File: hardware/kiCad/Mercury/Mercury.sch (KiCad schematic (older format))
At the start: 75 parts, among them J1 SWD, J10 OUTPUT, J11 Analog I/O, J12 Power Rails, J2 UART1, J3 I2C2, J4 UART1, J5 SPI1, J6 SPI2, J7 629105150521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

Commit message: Refresh
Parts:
- removed R24, R25: 22, Resistor_SMD:R_0402_1005Metric, symbol Device:R_Small
- H1, H2, H3, H4: footprint MountingHole:MountingHole_4.3mm_M4_Pad_Via -> MountingHole:MountingHole_3mm_Pad_Via
- J3: footprint Connector_Wire:SolderWire-0.1sqmm_1x04_P3.6mm_D0.4mm_OD1mm_Relief -> Connector_Wire:SolderWire-0.1sqmm_1x04_P3.6mm_D0.4mm_OD1mm
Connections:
- net ALT_INT_1: now also R8.1; no longer R9.1
- net ALT_INT_2: now also R9.1; no longer R8.1
- net FLASH_CS: now also R22.1; no longer R23.1
- net GPS_LNA_EN: now also U1.3 (PE4); no longer U1.65 (PC8)
- net I2C1_SCL: now also R5.1; no longer R4.1
- net I2C1_SDA: now also R4.1; no longer R5.1
- net SPI2_MISO: now also R23.1; no longer R21.1
- net SPI2_MOSI: now also R20.1; no longer R22.1
- net SPI2_SCK: now also R21.1; no longer R20.1
- net TIME_PULSE: now also U1.4 (PE5); no longer U1.66 (PC9)
- net USB_D+: now also J7.3 (D+)
- net USB_D-: now also J7.2 (D-)
- net ~GPS_RESET: now also U1.2 (PE3); no longer U1.67 (PA8)
- net ~GPS_SAFEBOOT: now also U1.5 (PE6); no longer U1.64 (PC7)
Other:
- moved on the sheet: J7
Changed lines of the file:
@@
 Wire Wire Line
 	5550 1000 5550 1100
+Text GLabel 8300 1250 0    50   Input ~ 0
+I2C1_SCL
 Text GLabel 8300 1150 0    50   Input ~ 0
-I2C1_SCL
-Text GLabel 8300 1250 0    50   Input ~ 0
 I2C1_SDA
 Text GLabel 9500 975  0    50   Input ~ 0
@@
 	1    0    0    -1
 $EndComp
-NoConn ~ 9675 2900
-Wire Wire Line
-	9475 2700 9425 2700
-Wire Wire Line
-	9475 2800 9425 2800
-$Comp
-L Device:R_Small R24
-U 1 1 5FE85A1A
-P 9575 2700
-F 0 "R24" V 9575 2700 50  0000 C CNN
-F 1 "22" V 9675 2700 50  0000 C CNN
-F 2 "Resistor_SMD:R_0402_1005Metric" H 9575 2700 50  0001 C CNN
-F 3 "~" H 9575 2700 50  0001 C CNN
-	1    9575 2700
-	0    -1   -1   0
-$EndComp
-$Comp
-L Device:R_Small R25
-U 1 1 5FE850CF
-P 9575 2800
-F 0 "R25" V 9575 2800 50  0000 C CNN
-F 1 "22" V 9475 2800 50  0000 C CNN
-F 2 "Resistor_SMD:R_0402_1005Metric" H 9575 2800 50  0001 C CNN
-F 3 "~" H 9575 2800 50  0001 C CNN
-	1    9575 2800
-	0    -1   -1   0
-$EndComp
-NoConn ~ 9675 2600
-Text GLabel 9425 2800 0    50   Input ~ 0
+NoConn ~ 9350 2875
+Wire Wire Line
+	9350 2675 9300 2675
+Wire Wire Line
+	9350 2775 9300 2775
+NoConn ~ 9350 2575
+Text GLabel 9300 2775 0    50   Input ~ 0
 USB_D+
-Text GLabel 9425 2700 0    50   Input ~ 0
+Text GLabel 9300 2675 0    50   Input ~ 0
 USB_D-
 $Comp
 L power:GND #PWR0138
 U 1 1 5FE68EC5
-P 9500 3000
-F 0 "#PWR0138" H 9500 2750 50  0001 C CNN
-F 1 "GND" H 9505 2827 50  0000 C CNN
-F 2 "" H 9500 3000 50  0001 C CNN
-F 3 "" H 9500 3000 50  0001 C CNN
-	1    9500 3000
+P 9175 2975
+F 0 "#PWR0138" H 9175 2725 50  0001 C CNN
+F 1 "GND" H 9180 2802 50  0000 C CNN
+F 2 "" H 9175 2975 50  0001 C CNN
+F 3 "" H 9175 2975 50  0001 C CNN
+	1    9175 2975
 	1    0    0    -1
 $EndComp
@@
 Text GLabel 2500 5000 0    50   Input ~ 0
 ALT_INT_1
-Text GLabel 4300 2600 2    50   Input ~ 0
+Text GLabel 2500 3800 0    50   Input ~ 0
 ~GPS_RESET
-Text GLabel 4300 6100 2    50   Input ~ 0
+Text GLabel 2500 4000 0    50   Input ~ 0
 TIME_PULSE
-Text GLabel 4300 6000 2    50   Input ~ 0
+Text GLabel 2500 3900 0    50   Input ~ 0
 GPS_LNA_EN
 Text GLabel 4300 5600 2    50   Input ~ 0
@@
 Wire Wire Line
 	9700 1175 9750 1175
+Text GLabel 9500 1275 0    50   Input ~ 0
+ALT_INT_2
 Text GLabel 9500 1175 0    50   Input ~ 0
-ALT_INT_2
-Text GLabel 9500 1275 0    50   Input ~ 0
 ALT_INT_1
 $Comp
@@
 Wire Wire Line
 	7450 3000 7500 3000
+Text GLabel 7175 2900 0    50   Input ~ 0
+SPI2_SCK
+Wire Wire Line
+	7175 2800 7250 2800
+Text GLabel 7175 3100 0    50   Input ~ 0
+SPI2_MISO
+Wire Wire Line
+	7175 2900 7250 2900
 Text GLabel 7175 2800 0    50   Input ~ 0
-SPI2_SCK
-Wire Wire Line
-	7175 2800 7250 2800
-Text GLabel 7175 2900 0    50   Input ~ 0
-SPI2_MISO
-Wire Wire Line
-	7175 2900 7250 2900
+SPI2_MOSI
+Wire Wire Line
+	7175 3000 7250 3000
+Wire Wire Line
+	7175 3100 7250 3100
 Text GLabel 7175 3000 0    50   Input ~ 0
-SPI2_MOSI
-Wire Wire Line
-	7175 3000 7250 3000
-Wire Wire Line
-	7175 3100 7250 3100
-Text GLabel 7175 3100 0    50   Input ~ 0
 FLASH_CS
 Text GLabel 2500 5800 0    50   Input ~ 0
@@
 NoConn ~ 2500 3600
 NoConn ~ 2500 3700
-NoConn ~ 2500 3800
-NoConn ~ 2500 3900
-NoConn ~ 2500 4000
-NoConn ~ 2500 4100
+NoConn ~ 4300 5900
 NoConn ~ 2500 4300
 NoConn ~ 2500 4400
@@
 Wire Wire Line
 	7575 1000 7500 1000
-Text GLabel 4300 5900 2    50   Input ~ 0
+Text GLabel 2500 4100 0    50   Input ~ 0
 ~GPS_SAFEBOOT
 $Comp
@@
 F 0 "H1" V 8404 4250 50  0000 L CNN
 F 1 "MountingHole_Pad" V 8495 4250 50  0000 L CNN
-F 2 "MountingHole:MountingHole_4.3mm_M4_Pad_Via" H 8450 4100 50  0001 C CNN
+F 2 "MountingHole:MountingHole_3mm_Pad_Via" H 8450 4100 50  0001 C CNN
 F 3 "~" H 8450 4100 50  0001 C CNN
 	1    8450 4100
@@
 F 0 "H2" V 8404 4475 50  0000 L CNN
 F 1 "MountingHole_Pad" V 8495 4475 50  0000 L CNN
-F 2 "MountingHole:MountingHole_4.3mm_M4_Pad_Via" H 8450 4325 50  0001 C CNN
+F 2 "MountingHole:MountingHole_3mm_Pad_Via" H 8450 4325 50  0001 C CNN
 F 3 "~" H 8450 4325 50  0001 C CNN
 	1    8450 4325
@@
 F 0 "H3" V 8404 4725 50  0000 L CNN
 F 1 "MountingHole_Pad" V 8495 4725 50  0000 L CNN
-F 2 "MountingHole:MountingHole_4.3mm_M4_Pad_Via" H 8450 4575 50  0001 C CNN
+F 2 "MountingHole:MountingHole_3mm_Pad_Via" H 8450 4575 50  0001 C CNN
 F 3 "~" H 8450 4575 50  0001 C CNN
 	1    8450 4575
@@
 F 0 "H4" V 8404 4950 50  0000 L CNN
 F 1 "MountingHole_Pad" V 8495 4950 50  0000 L CNN
-F 2 "MountingHole:MountingHole_4.3mm_M4_Pad_Via" H 8450 4800 50  0001 C CNN
+F 2 "MountingHole:MountingHole_3mm_Pad_Via" H 8450 4800 50  0001 C CNN
 F 3 "~" H 8450 4800 50  0001 C CNN
 	1    8450 4800
@@
 L 629105150521:629105150521 J7
 U 1 1 5FF1E6CB
-P 10075 2800
-F 0 "J7" H 10367 2839 50  0000 L CNN
-F 1 "629105150521" H 9775 2425 50  0000 L CNN
-F 2 "629105150521:629105150521" H 10075 2800 50  0001 L BNN
-F 3 "" H 10075 2800 50  0001 L BNN
-F 4 "629105150521" H 10075 2800 50  0001 L BNN "VALUE"
-F 5 "5" H 10075 2800 50  0001 L BNN "PINS"
-F 6 "Type B" H 10075 2800 50  0001 L BNN "INTERFACE-TYPE"
-F 7 "Horizontal" H 10075 2800 50  0001 L BNN "TYPE"
-F 8 "Receptacle" H 10075 2800 50  0001 L BNN "GERDER"
-F 9 "SMT" H 10075 2800 50  0001 L BNN "MOUNT"
-F 10 "30V(AC)" H 10075 2800 50  0001 L BNN "WORKING-VOLTAGE"
-F 11 "Tape and Reel" H 10075 2800 50  0001 L BNN "PACKAGING"
-F 12 "3.0A" H 10075 2800 50  0001 L BNN "IR1"
-F 13 "629105150521" H 10075 2800 50  0001 L BNN "PART-NUMBER"
-F 14 "https://www.we-online.com/catalog/datasheet/629105150521.pdf" H 10075 2800 50  0001 L BNN "DATASHEET-URL"
-F 15 "Micro USB 2.0" H 10075 2800 50  0001 L BNN "APPLICATION"
-	1    10075 2800
-	1    0    0    -1
-$EndComp
-Wire Wire Line
-	9500 3000 9675 3000
+P 9750 2775
+F 0 "J7" H 10042 2814 50  0000 L CNN
+F 1 "629105150521" H 9450 2400 50  0000 L CNN
+F 2 "629105150521:629105150521" H 9750 2775 50  0001 L BNN
+F 3 "" H 9750 2775 50  0001 L BNN
+F 4 "629105150521" H 9750 2775 50  0001 L BNN "VALUE"
+F 5 "5" H 9750 2775 50  0001 L BNN "PINS"
+F 6 "Type B" H 9750 2775 50  0001 L BNN "INTERFACE-TYPE"
+F 7 "Horizontal" H 9750 2775 50  0001 L BNN "TYPE"
+F 8 "Receptacle" H 9750 2775 50  0001 L BNN "GERDER"
+F 9 "SMT" H 9750 2775 50  0001 L BNN "MOUNT"
+F 10 "30V(AC)" H 9750 2775 50  0001 L BNN "WORKING-VOLTAGE"
+F 11 "Tape and Reel" H 9750 2775 50  0001 L BNN "PACKAGING"
+F 12 "3.0A" H 9750 2775 50  0001 L BNN "IR1"
+F 13 "629105150521" H 9750 2775 50  0001 L BNN "PART-NUMBER"
+F 14 "https://www.we-online.com/catalog/datasheet/629105150521.pdf" H 9750 2775 50  0001 L BNN "DATASHEET-URL"
+F 15 "Micro USB 2.0" H 9750 2775 50  0001 L BNN "APPLICATION"
+	1    9750 2775
+	1    0    0    -1
+$EndComp
+Wire Wire Line
+	9175 2975 9350 2975
 $Comp
 L power:PWR_FLAG #FLG0104
@@
 $EndComp
 Connection ~ 3600 7050
-NoConn ~ 9675 3100
+NoConn ~ 9350 3075
 NoConn ~ 4300 2700
 NoConn ~ 4300 2800
@@
 F 0 "J3" H 10030 1067 50  0000 L CNN
 F 1 "I2C2" H 10030 976 50  0000 L CNN
-F 2 "Connector_Wire:SolderWire-0.1sqmm_1x04_P3.6mm_D0.4mm_OD1mm_Relief" H 9950 1075 50  0001 C CNN
+F 2 "Connector_Wire:SolderWire-0.1sqmm_1x04_P3.6mm_D0.4mm_OD1mm" H 9950 1075 50  0001 C CNN
 F 3 "~" H 9950 1075 50  0001 C CNN
 	1    9950 1075
 	1    0    0    -1
 $EndComp
+NoConn ~ 4300 6000
+NoConn ~ 4300 6100
+NoConn ~ 4300 2600
 $EndSCHEMATC

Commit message: Layout Done
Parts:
- removed J3: I2C2, Connector_Wire:SolderWire-0.1sqmm_1x04_P3.6mm_D0.4mm_OD1mm, symbol Connector_Generic:Conn_01x04
- removed R9: 22, Resistor_SMD:R_0402_1005Metric, symbol Device:R_Small
- added J3: I2C2, Connector_Wire:SolderWire-0.1sqmm_1x03_P3.6mm_D0.4mm_OD1mm, symbol Connector_Generic:Conn_01x03
- J8: footprint TerminalBlock_Phoenix:TerminalBlock_Phoenix_MKDS-3-2-5.08_1x02_P5.08mm_Horizontal -> TerminalBlock_Phoenix:TerminalBlock_Phoenix_MKDS-1,5-2-5.08_1x02_P5.08mm_Horizontal
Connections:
- net RF_CS: now also R16.1; no longer R19.1
- net SPI1_MOSI: now also R19.1; no longer R18.1
- net SPI1_SCK: now also R18.1; no longer R16.1
- net at R6.2: now also J3.1 (Pin_1)
- net at R7.2: now also J3.2 (Pin_2)
- net at R8.2: now also J3.3 (Pin_3)
- net ALT_INT_2: no longer names the net of U1.45 (PE14)
- no-connect marks 46 -> 48
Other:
- moved on the sheet: R6, R7, R8
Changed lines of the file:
@@
 F 0 "J8" H 8650 1600 50  0000 L CNN
 F 1 "Battery Input" H 8450 1900 50  0000 L CNN
-F 2 "TerminalBlock_Phoenix:TerminalBlock_Phoenix_MKDS-3-2-5.08_1x02_P5.08mm_Horizontal" H 8700 1800 50  0001 C CNN
+F 2 "TerminalBlock_Phoenix:TerminalBlock_Phoenix_MKDS-1,5-2-5.08_1x02_P5.08mm_Horizontal" H 8700 1800 50  0001 C CNN
 F 3 "~" H 8700 1800 50  0001 C CNN
 	1    8700 1800
@@
 Text GLabel 8300 1150 0    50   Input ~ 0
 I2C1_SDA
-Text GLabel 9500 975  0    50   Input ~ 0
+Text GLabel 9575 1100 0    50   Input ~ 0
 I2C2_SCL
 Text GLabel 9450 1850 0    50   Input ~ 0
@@
 L Device:R_Small R6
 U 1 1 5FEBD667
-P 9600 975
-F 0 "R6" V 9600 925 50  0000 L CNN
-F 1 "22" V 9650 800 50  0000 L CNN
-F 2 "Resistor_SMD:R_0402_1005Metric" H 9600 975 50  0001 C CNN
-F 3 "~" H 9600 975 50  0001 C CNN
-	1    9600 975
+P 9675 1100
+F 0 "R6" V 9675 1050 50  0000 L CNN
+F 1 "22" V 9725 925 50  0000 L CNN
+F 2 "Resistor_SMD:R_0402_1005Metric" H 9675 1100 50  0001 C CNN
+F 3 "~" H 9675 1100 50  0001 C CNN
+	1    9675 1100
 	0    -1   -1   0
 $EndComp
@@
 L Device:R_Small R7
 U 1 1 5FEBDD35
-P 9600 1075
-F 0 "R7" V 9600 1025 50  0000 L CNN
-F 1 "22" V 9650 900 50  0000 L CNN
-F 2 "Resistor_SMD:R_0402_1005Metric" H 9600 1075 50  0001 C CNN
-F 3 "~" H 9600 1075 50  0001 C CNN
-	1    9600 1075
+P 9675 1200
+F 0 "R7" V 9675 1150 50  0000 L CNN
+F 1 "22" V 9725 1025 50  0000 L CNN
+F 2 "Resistor_SMD:R_0402_1005Metric" H 9675 1200 50  0001 C CNN
+F 3 "~" H 9675 1200 50  0001 C CNN
+	1    9675 1200
 	0    -1   -1   0
 $EndComp
 Text GLabel 8425 6500 2    50   Input ~ 0
 I2C2_SDA
-Text GLabel 9500 1075 0    50   Input ~ 0
+Text GLabel 9575 1200 0    50   Input ~ 0
 I2C2_SDA
 $Comp
@@
 Text GLabel 4300 4700 2    50   Input ~ 0
 FLASH_CS
-Text GLabel 2500 4900 0    50   Input ~ 0
-ALT_INT_2
 Text GLabel 2500 5000 0    50   Input ~ 0
 ALT_INT_1
@@
 RF_GPO0
 Wire Wire Line
-	9700 1075 9750 1075
-Wire Wire Line
-	9700 975  9750 975
+	9775 1200 9825 1200
+Wire Wire Line
+	9775 1100 9825 1100
 $Comp
 L Device:R_Small R8
 U 1 1 5FECDB5E
-P 9600 1175
-F 0 "R8" V 9600 1125 50  0000 L CNN
-F 1 "22" V 9650 1000 50  0000 L CNN
-F 2 "Resistor_SMD:R_0402_1005Metric" H 9600 1175 50  0001 C CNN
-F 3 "~" H 9600 1175 50  0001 C CNN
-	1    9600 1175
-	0    -1   -1   0
-$EndComp
-$Comp
-L Device:R_Small R9
-U 1 1 5FECDB68
-P 9600 1275
-F 0 "R9" V 9600 1225 50  0000 L CNN
-F 1 "22" V 9650 1100 50  0000 L CNN
-F 2 "Resistor_SMD:R_0402_1005Metric" H 9600 1275 50  0001 C CNN
-F 3 "~" H 9600 1275 50  0001 C CNN
-	1    9600 1275
-	0    -1   -1   0
-$EndComp
-Wire Wire Line
-	9700 1275 9750 1275
-Wire Wire Line
-	9700 1175 9750 1175
-Text GLabel 9500 1275 0    50   Input ~ 0
-ALT_INT_2
-Text GLabel 9500 1175 0    50   Input ~ 0
+P 9675 1300
+F 0 "R8" V 9675 1250 50  0000 L CNN
+F 1 "22" V 9725 1125 50  0000 L CNN
+F 2 "Resistor_SMD:R_0402_1005Metric" H 9675 1300 50  0001 C CNN
+F 3 "~" H 9675 1300 50  0001 C CNN
+	1    9675 1300
+	0    -1   -1   0
+$EndComp
+Wire Wire Line
+	9775 1300 9825 1300
+Text GLabel 9575 1300 0    50   Input ~ 0
 ALT_INT_1
 $Comp
@@
 Wire Wire Line
 	5975 3025 6025 3025
-Text GLabel 5700 2825 0    50   Input ~ 0
+Text GLabel 5700 3025 0    50   Input ~ 0
 SPI1_SCK
 Wire Wire Line
@@
 Wire Wire Line
 	5700 2925 5775 2925
-Text GLabel 5700 3025 0    50   Input ~ 0
+Text GLabel 5700 3125 0    50   Input ~ 0
 SPI1_MOSI
 Wire Wire Line
 	5700 3025 5775 3025
-Text GLabel 5700 3125 0    50   Input ~ 0
+Text GLabel 5700 2825 0    50   Input ~ 0
 RF_CS
 Wire Wire Line
@@
 	1    0    0    -1
 $EndComp
-$Comp
-L Connector_Generic:Conn_01x04 J3
-U 1 1 60266721
-P 9950 1075
-F 0 "J3" H 10030 1067 50  0000 L CNN
-F 1 "I2C2" H 10030 976 50  0000 L CNN
-F 2 "Connector_Wire:SolderWire-0.1sqmm_1x04_P3.6mm_D0.4mm_OD1mm" H 9950 1075 50  0001 C CNN
-F 3 "~" H 9950 1075 50  0001 C CNN
-	1    9950 1075
-	1    0    0    -1
-$EndComp
 NoConn ~ 4300 6000
 NoConn ~ 4300 6100
 NoConn ~ 4300 2600
+NoConn ~ 2500 4900
+NoConn ~ 10375 3850
+$Comp
+L Connector_Generic:Conn_01x03 J3
+U 1 1 600074F1
+P 10025 1200
+F 0 "J3" H 10105 1242 50  0000 L CNN
+F 1 "I2C2" H 10105 1151 50  0000 L CNN
+F 2 "Connector_Wire:SolderWire-0.1sqmm_1x03_P3.6mm_D0.4mm_OD1mm" H 10025 1200 50  0001 C CNN
+F 3 "~" H 10025 1200 50  0001 C CNN
+	1    10025 1200
+	1    0    0    -1
+$EndComp
 $EndSCHEMATC

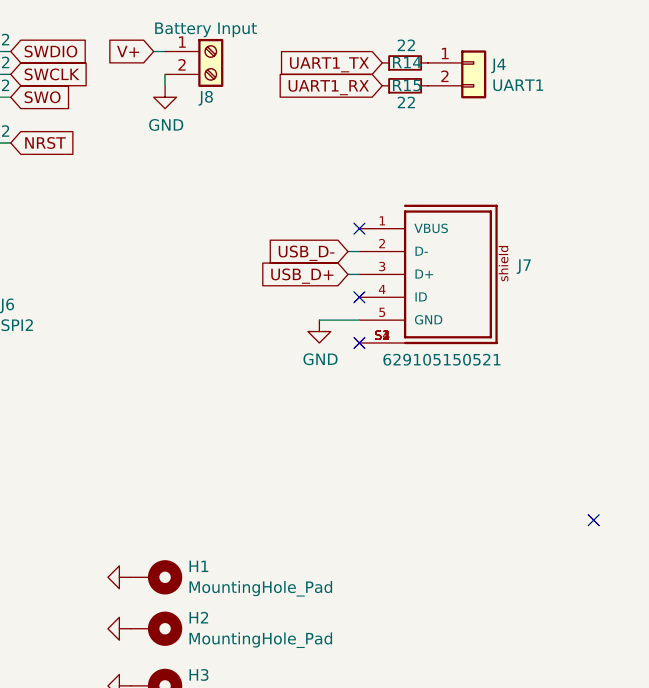
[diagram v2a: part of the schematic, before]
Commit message: Added USB
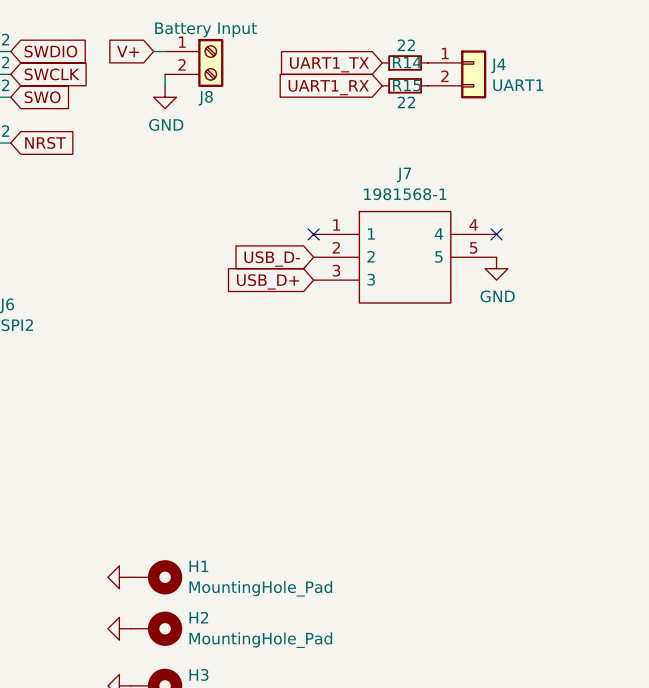
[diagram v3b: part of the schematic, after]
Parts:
- removed J7: 629105150521, 629105150521:629105150521, symbol 629105150521:629105150521
- added J7: 1981568-1, USB:1981568-1, symbol USB:1981568-1
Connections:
- net GND: now also J7.5
- net USB_D+: now also J7.3
- net USB_D-: now also J7.2
- no-connect marks 48 -> 46
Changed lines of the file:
@@
 	1    0    0    -1
 $EndComp
-NoConn ~ 9350 2875
-Wire Wire Line
-	9350 2675 9300 2675
-Wire Wire Line
-	9350 2775 9300 2775
-NoConn ~ 9350 2575
-Text GLabel 9300 2775 0    50   Input ~ 0
+NoConn ~ 9150 2600
+Text GLabel 9150 2800 0    50   Input ~ 0
 USB_D+
-Text GLabel 9300 2675 0    50   Input ~ 0
+Text GLabel 9150 2700 0    50   Input ~ 0
 USB_D-
 $Comp
 L power:GND #PWR0138
 U 1 1 5FE68EC5
-P 9175 2975
-F 0 "#PWR0138" H 9175 2725 50  0001 C CNN
-F 1 "GND" H 9180 2802 50  0000 C CNN
-F 2 "" H 9175 2975 50  0001 C CNN
-F 3 "" H 9175 2975 50  0001 C CNN
-	1    9175 2975
+P 9950 2700
+F 0 "#PWR0138" H 9950 2450 50  0001 C CNN
+F 1 "GND" H 9955 2527 50  0000 C CNN
+F 2 "" H 9950 2700 50  0001 C CNN
+F 3 "" H 9950 2700 50  0001 C CNN
+	1    9950 2700
 	1    0    0    -1
 $EndComp
@@
 $EndComp
 $Comp
-L 629105150521:629105150521 J7
-U 1 1 5FF1E6CB
-P 9750 2775
-F 0 "J7" H 10042 2814 50  0000 L CNN
-F 1 "629105150521" H 9450 2400 50  0000 L CNN
-F 2 "629105150521:629105150521" H 9750 2775 50  0001 L BNN
-F 3 "" H 9750 2775 50  0001 L BNN
-F 4 "629105150521" H 9750 2775 50  0001 L BNN "VALUE"
-F 5 "5" H 9750 2775 50  0001 L BNN "PINS"
-F 6 "Type B" H 9750 2775 50  0001 L BNN "INTERFACE-TYPE"
-F 7 "Horizontal" H 9750 2775 50  0001 L BNN "TYPE"
-F 8 "Receptacle" H 9750 2775 50  0001 L BNN "GERDER"
-F 9 "SMT" H 9750 2775 50  0001 L BNN "MOUNT"
-F 10 "30V(AC)" H 9750 2775 50  0001 L BNN "WORKING-VOLTAGE"
-F 11 "Tape and Reel" H 9750 2775 50  0001 L BNN "PACKAGING"
-F 12 "3.0A" H 9750 2775 50  0001 L BNN "IR1"
-F 13 "629105150521" H 9750 2775 50  0001 L BNN "PART-NUMBER"
-F 14 "https://www.we-online.com/catalog/datasheet/629105150521.pdf" H 9750 2775 50  0001 L BNN "DATASHEET-URL"
-F 15 "Micro USB 2.0" H 9750 2775 50  0001 L BNN "APPLICATION"
-	1    9750 2775
-	1    0    0    -1
-$EndComp
-Wire Wire Line
-	9175 2975 9350 2975
-$Comp
 L power:PWR_FLAG #FLG0104
 U 1 1 5FF0389D
@@
 $EndComp
 Connection ~ 3600 7050
-NoConn ~ 9350 3075
+NoConn ~ 9950 2600
 NoConn ~ 4300 2700
 NoConn ~ 4300 2800
@@
 NoConn ~ 4300 2600
 NoConn ~ 2500 4900
-NoConn ~ 10375 3850
 $Comp
 L Connector_Generic:Conn_01x03 J3
@@
 	1    0    0    -1
 $EndComp
+$Comp
+L USB:1981568-1 J7
+U 1 1 5FF66D02
+P 9150 2600
+F 0 "J7" H 9550 2865 50  0000 C CNN
+F 1 "1981568-1" H 9550 2774 50  0000 C CNN
+F 2 "USB:1981568-1" H 9800 2700 50  0001 L CNN
+F 3 "http://www.te.com/commerce/DocumentDelivery/DDEController?Action=srchrtrv&DocNm=1981568&DocType=Customer+Drawing&DocLang=English" H 9800 2600 50  0001 L CNN
+F 4 "REC TYPE B ASSY (Au) MICRO USB" H 9800 2500 50  0001 L CNN "Description"
+F 5 "" H 9800 2400 50  0001 L CNN "Height"
+F 6 "571-1981568-1" H 9800 2300 50  0001 L CNN "Mouser Part Number"
+F 7 "https://www.mouser.co.uk/ProductDetail/TE-Connectivity/1981568-1?qs=zxTme0yW%2FbaAfvOKTKC5hw%3D%3D" H 9800 2200 50  0001 L CNN "Mouser Price/Stock"
+F 8 "TE Connectivity" H 9800 2100 50  0001 L CNN "Manufacturer_Name"
+F 9 "1981568-1" H 9800 2000 50  0001 L CNN "Manufacturer_Part_Number"
+	1    9150 2600
+	1    0    0    -1
+$EndComp

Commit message: Layout + Routing v1 done
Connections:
- net AGPIO1: now also J11.2 (Pin_2); no longer J11.1 (Pin_1)
- net AGPIO2: now also J11.1 (Pin_1); no longer J11.2 (Pin_2)
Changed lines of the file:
@@
 	1    0    0    -1
 $EndComp
+Text GLabel 6025 4725 0    50   Input ~ 0
+AGPIO1
 Text GLabel 6025 4625 0    50   Input ~ 0
-AGPIO1
-Text GLabel 6025 4725 0    50   Input ~ 0
 AGPIO2
 Text GLabel 6025 4225 0    50   Input ~ 0

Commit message: Sent For Manufacture
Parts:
- C1: LCSC Part # (none) -> C1779
- C10: LCSC Part # (none) -> C15195
- C11, C12: LCSC Part # (none) -> C23630
- C13, C14: LCSC Part # (none) -> C1547
- C15, C16, C17, C18: LCSC Part # (none) -> C45783
- C2, C3, C4, C5, C6, C7, C8: LCSC Part # (none) -> C1525
- C9: LCSC Part # (none) -> C52923
- D1: LCSC Part # (none) -> C72043
- D2: LCSC Part # (none) -> C2286
- D3: LCSC Part # (none) -> C375450
- J7: symbol USB:1981568-1 -> Mercury-rescue:1981568-1-USB
- L1: LCSC Part # (none) -> C26443
- Q1: LCSC Part # (none) -> C15127
- R1: LCSC Part # (none) -> C25744
- R10, R11, R12, R13, R14, R15, R16, R17, R18, R19, R20, R21, R22, R23, R4, R5, R6, R7, R8: LCSC Part # (none) -> C25092
- R2: LCSC Part # (none) -> C17714
- R26, R27, R28, R29: LCSC Part # (none) -> C25900
- R3, R30: LCSC Part # (none) -> C11702
- R31: value 4.7k -> 4k7; LCSC Part # (none) -> C25900
- U1: LCSC Part # (none) -> C12345
- U2: LCSC Part # (none) -> C6186
- U3: LCSC Part # (none) -> C6187
- Y1: LCSC Part # (none) -> C13738
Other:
- moved on the sheet: H1, H2, H3, H4
